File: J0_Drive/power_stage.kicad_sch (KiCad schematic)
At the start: 0 parts

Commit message: finished first design of power stage page
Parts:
- added C6, C7, C8: 220nF, symbol Device:C
- added D1, D2, D3, D4, D5, D6: BAT43W-V, Diode_SMD:D_SOD-123, symbol Diode:BAT43W-V
- added Q1, Q2, Q3, Q4, Q5, Q6: STL110N10F7, MOSFET_10N10F7_STM, symbol J0_Drive_Symbols:STL110N10F7
- added R10, R15, R20: 0.001, symbol Device:R
- added R11, R12, R16, R17, R6, R8: 33, symbol Device:R
- added R13, R14, R18, R19, R7, R9: 22k, symbol Device:R
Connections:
- new net: D6.2 (A), Q6.4 (G), R17.2, R19.1
- new net: D3.2 (A), Q3.4 (G), R11.2, R13.1
- new net: D5.2 (A), Q5.4 (G), R16.2, R18.1
- new net: D4.2 (A), Q4.4 (G), R12.2, R14.1
- new net: D1.2 (A), Q1.4 (G), R6.2, R7.1
- new net: D2.2 (A), Q2.4 (G), R8.2, R9.1
- new net GHS1: D1.1 (K), R6.1
- new net GHS2: D3.1 (K), D5.1 (K), R11.1, R16.1
- new net GLS1: D2.1 (K), R8.1
- new net GLS2: D4.1 (K), D6.1 (K), R12.1, R17.1
- new net GND: C6.2, C7.2, C8.2, Q2.1 (S), Q2.2 (S), Q2.3 (S), Q4.1 (S), Q4.2 (S), Q4.3 (S), Q6.1 (S), Q6.2 (S), Q6.3 (S), R14.2, R19.2, R9.2
- new net PHASE_1: R10.1, R20.1
- new net PHASE_2: R15.1
- new net SNS1_P: Q1.1 (S), Q1.2 (S), Q1.3 (S), Q2.5 (D), Q2.6 (D), Q2.7 (D), Q2.8 (D), Q5.1 (S), Q5.2 (S), Q5.3 (S), Q6.5 (D), Q6.6 (D), Q6.7 (D), Q6.8 (D), R10.2, R18.2, R20.2, R7.2
- new net SNS2_P: Q3.1 (S), Q3.2 (S), Q3.3 (S), Q4.5 (D), Q4.6 (D), Q4.7 (D), Q4.8 (D), R13.2, R15.2
- new net VM: C6.1, C7.1, C8.1, Q1.5 (D), Q1.6 (D), Q1.7 (D), Q1.8 (D), Q3.5 (D), Q3.6 (D), Q3.7 (D), Q3.8 (D), Q5.5 (D), Q5.6 (D), Q5.7 (D), Q5.8 (D)
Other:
- note added: "Differential pair"
- note added: "Inline current sense"
- note added: "R_shunt = V_OUTmax_deviation/(gain*I_max) = 1/(20*40) = 0.00125Ohm = 1.25mOhm 1mOhm shunt resistor P=I^2*R = 40^2*(0.001) = 1.6W rated for more than 3W (margin)"
- note added: "validate gate resistor value on hardware"

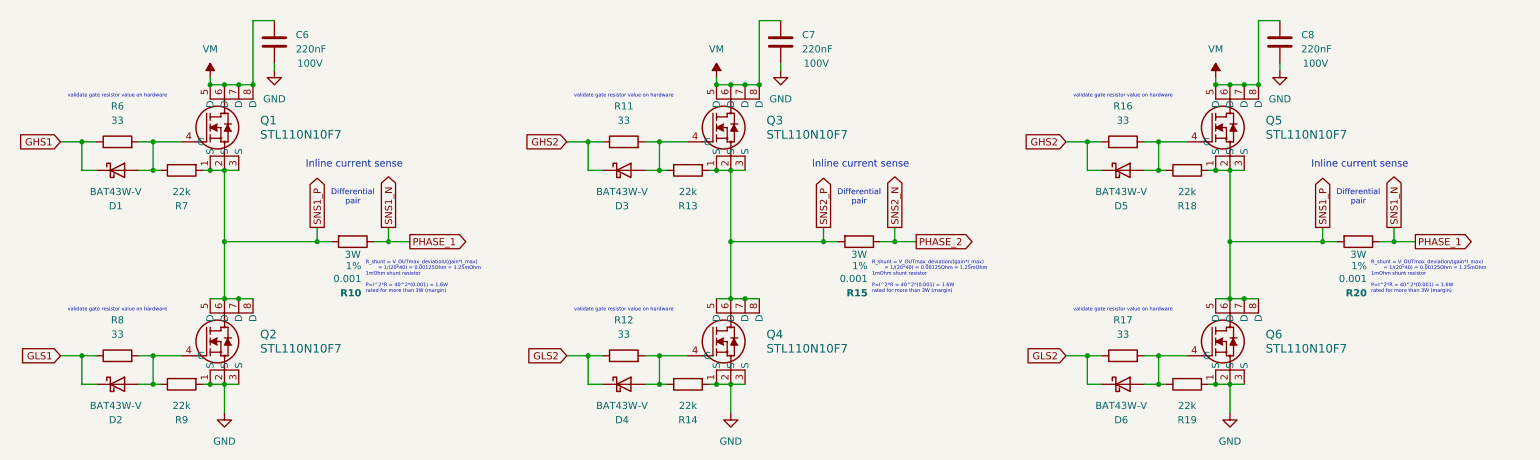
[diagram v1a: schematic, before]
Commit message: finished half bridges, started mcu
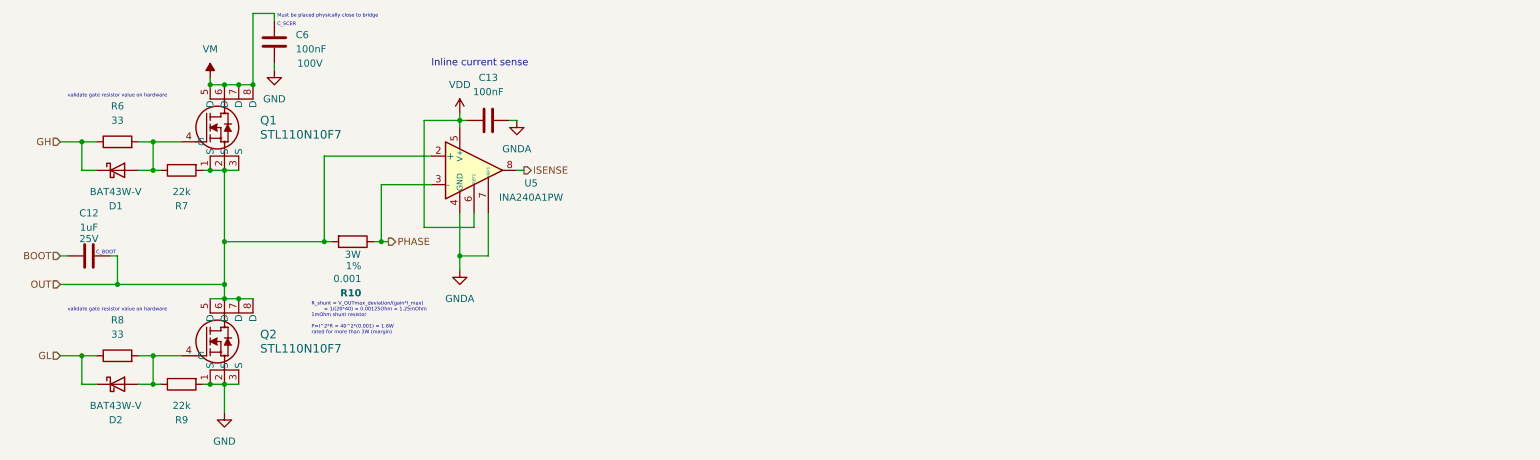
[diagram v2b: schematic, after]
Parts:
- removed C7, C8: 220nF, symbol Device:C
- removed D3, D4, D5, D6: BAT43W-V, Diode_SMD:D_SOD-123, symbol Diode:BAT43W-V
- removed Q3, Q4, Q5, Q6: STL110N10F7, MOSFET_10N10F7_STM, symbol J0_Drive_Symbols:STL110N10F7
- removed R11, R12, R16, R17: 33, symbol Device:R
- removed R13, R14, R18, R19: 22k, symbol Device:R
- removed R15, R20: 0.001, symbol Device:R
- added C12: 1uF, symbol Device:C
- added C13: 100nF, symbol Device:C
- added U5: INA240A1PW, Package_SO:TSSOP-8_4.4x3mm_P0.65mm, symbol Amplifier_Current:INA240A1PW
- C6: value 220nF -> 100nF
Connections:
- net GHS1 renamed GH
- net GLS1 renamed GL
- net PHASE_1 renamed PHASE
- net PHASE: now also U5.3 (-)
- net SNS1_P renamed OUT
- net OUT: now also C12.2, U5.2 (+)
- new net BOOT: C12.1
- new net GNDA: C13.2, U5.1 (GND), U5.4 (GND), U5.7 (REF1)
- new net ISENSE: U5.8
- new net VDD: C13.1, U5.5 (V+), U5.6 (REF2)
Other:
- note added: "C_BOOT"
- note added: "C_SCER"
- note added: "Must be placed physically close to bridge"
- note removed: "Differential pair"
